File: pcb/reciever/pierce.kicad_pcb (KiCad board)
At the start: 2 copper layers, 22.3 x 51.3 mm, 7 parts

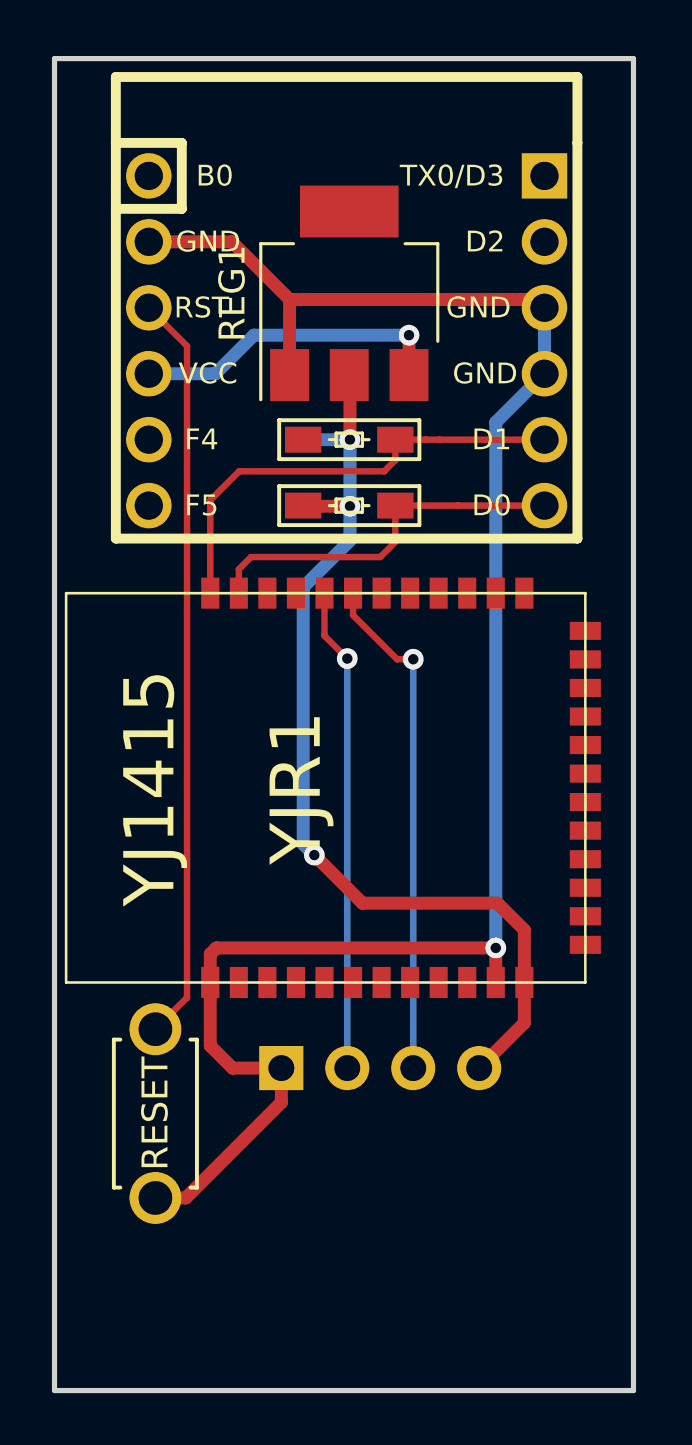
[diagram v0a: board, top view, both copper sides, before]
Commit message: add gnd planes
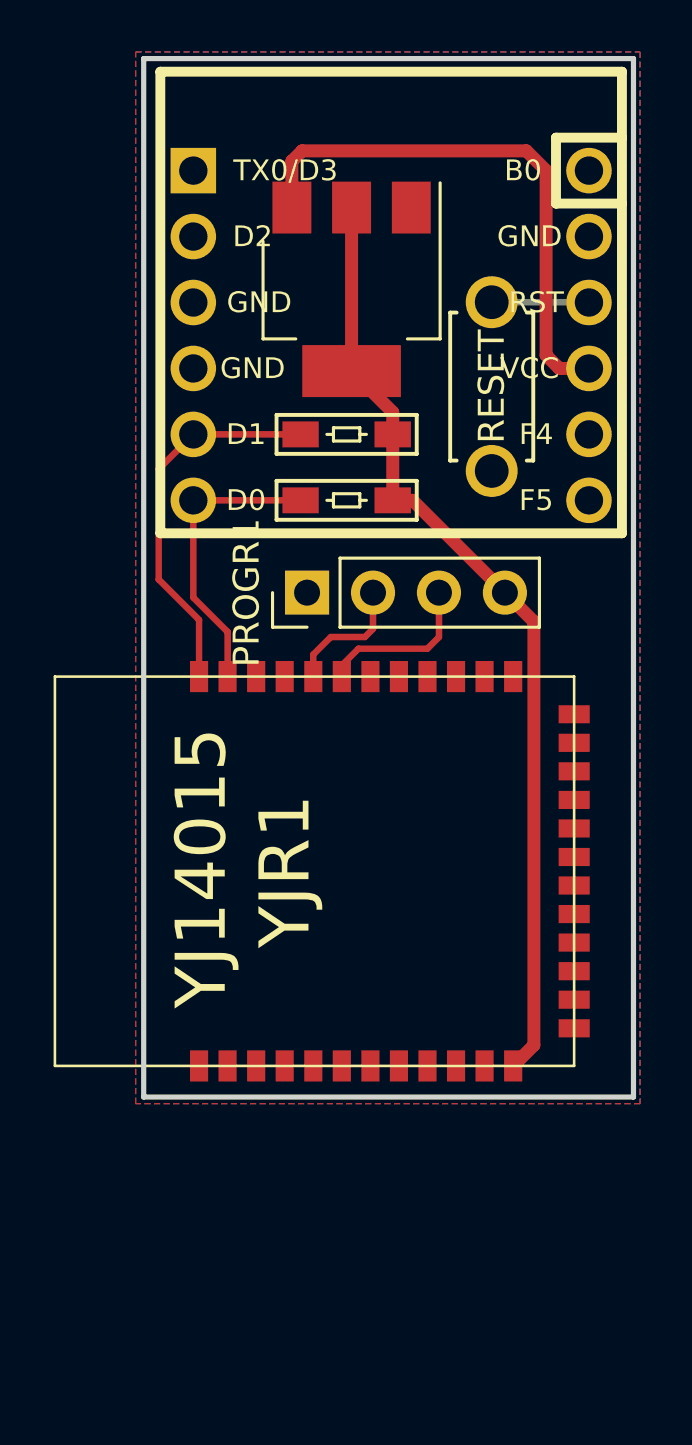
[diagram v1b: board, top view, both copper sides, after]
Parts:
- AVR1: moved to B.Cu
- PROGR1: footprint pierce:PinHeader_1x04_P2.54mm_Horizontal -> Connector_PinHeader_2.54mm:PinHeader_1x04_P2.54mm_Vertical; moved to F.Cu
- YJR1: value YJ1415 -> YJ14015
- moved RST1 30.9 mm to (151.2, 42.6)
- moved PROGR1 18.3 mm to (144.0, 50.6), turned to 90 degrees
- moved YJR1 3.24 mm to (154.3, 61.3)
- moved AVR1 2.23 mm to (147.5, 48.3), turned to 180 degrees
- moved R4 0.23 mm to (145.6, 47.0), turned to 0 degrees
- moved R5 0.23 mm to (145.6, 44.5), turned to 0 degrees
- moved REG1 0.18 mm to (145.8, 38.9), turned to 270 degrees
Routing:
- net GND: track 71.5 -> 0.00 mm, vias 1 -> 0
- net reset: track 28.9 -> 3.75 mm
- net CLKR: track 18.7 -> 4.96 mm, vias 1 -> 0
- net DIOR: track 19.6 -> 6.34 mm, vias 1 -> 0
- net VCC_5V: track 12.2 -> 21.0 mm, vias 1 -> 0
- net I2C_SDA: track 17.9 -> 14.7 mm
- net I2C_SCL: track 14.5 -> 11.5 mm
- net VCC_3.3V: track 38.4 -> 36.8 mm, vias 3 -> 0
- net Net-(AVR1-Pad19): track 0.00 -> 0.72 mm
- added copper zone on B.Cu, net GND
- added copper zone on F.Cu, net GND
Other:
- board size 22.3 x 51.3 mm -> 18.9 x 40 mm

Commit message: small visual adjustments
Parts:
- added REF**: OSHW-Logo2_7.3x6mm_SilkScreen, pierce:OSHW-Logo2_7.3x6mm_SilkScreen, B.Cu at (146.5, 63.3)
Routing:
- net GND: vias 0 -> 1
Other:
- board text added: "by durken"
- board text added: "pierce 2.0"
